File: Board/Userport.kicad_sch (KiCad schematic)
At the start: 8 parts, among them CN5 PORT_USER_PET_EDGE, X7 M09-182, X8 M09-182

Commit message: ultipet 1.1a board
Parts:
- removed JP18: JP2E, cbm_ultipet_v1:JP2, symbol cbm_ultipet_v1-eagle-import:JP2E
- added C147, C150: 0.1u, cbm_ultipet_v1:C0603, symbol cbm_ultipet_v1-eagle-import:C-EUC0603
- added U4, U5: CD4053B, Package_SO:TSSOP-16_4.4x5mm_P0.65mm, symbol Analog_Switch:CD4053B
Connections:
- net GND: now also C147.2, C150.2, U4.6 (INH), U4.7 (VEE), U4.8 (VSS), U5.6 (INH), U5.7 (VEE), U5.8 (VSS)
- net UP0: now also U5.13 (A1), U5.2 (B0); no longer X7.1
- net UP1: now also U4.1 (B1), U4.5 (C0); no longer X7.2
- net UP2: now also U5.1 (B1), U5.12 (A0); no longer X7.4
- net UP3: now also U4.2 (B0), U4.3 (C1); no longer X7.3
- net UP5: now also U4.13 (A1)
- net VCC: now also C147.1, C150.1, U4.16 (VDD), U5.16 (VDD)
- net at X7.6: now also U4.14 (A)
- net at D29.A, D30.A: now also U4.12 (A0)
- new net: U5.15 (B), X7.1
- new net: U4.4 (C), X7.2
- new net: U5.14 (A), X7.3
- new net: U4.15 (B), X7.4
- new net FUC2: U4.10 (S2), U4.11 (S1), U4.9 (S3), U5.10 (S2), U5.11 (S1), U5.9 (S3)
- new net OPENHIGH: U5.4 (C)
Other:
- note added: "1.1A: - switch between single/dual joystick config - switch Joy1/Joy2 on board"
- note added: "CBM-ULTIPET-V1.1A"
- note added: "CBM-ULTIPET-V1.1A-20240601"
- note added: "Down"
- note added: "Fire"
- note added: "High is single Joystick, Low is dual Joystick"
- note added: "Left"
- note added: "Right"
- note added: "Up"
- note added: "Use Female connectors!"
- note removed: "CBM-ULTIPET-V1.0A"
- note removed: "CBM-ULTIPET-V1.0A-20240104"
- moved on the sheet: D27, D28, D29, D30, X7, X8

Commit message: various fixes as documented in github issues
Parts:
- removed D27, D28, D29, D30: 1N4148DO35-10, cbm_ultipet_v1:DO35-10, symbol cbm_ultipet_v1-eagle-import:1N4148DO35-10
- added D12, D15, D16, D17: 1N4448, cbm_ultipet_v1:DO35-10, symbol cbm_ultipet_v1-eagle-import:1N4148DO35-10
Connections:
- net UP0: now also D12.A
- net UP1: now also D15.A
- net UP4: now also D16.A
- net UP5: now also D17.A
- net at X8.6: now also D16.C, D17.C
- net at U4.12 (A0): now also D12.C, D15.C
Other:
- note added: "1.1A: - switch between single/dual joystick config - switch Joy1/Joy2 on board 1.2A: - switch diodes direction to fix dual mode joystick fire - replace 1N4148 with 1N4448 due to lower fwd voltage"
- note added: "CBM-ULTIPET-V1.2A"
- note added: "CBM-ULTIPET-V1.2A-20241013"
- note added: "Male DB9 connectors"
- note removed: "1.1A: - switch between single/dual joystick config - switch Joy1/Joy2 on board"
- note removed: "CBM-ULTIPET-V1.1A"
- note removed: "CBM-ULTIPET-V1.1A-20240601"
- note removed: "Use Female connectors!"

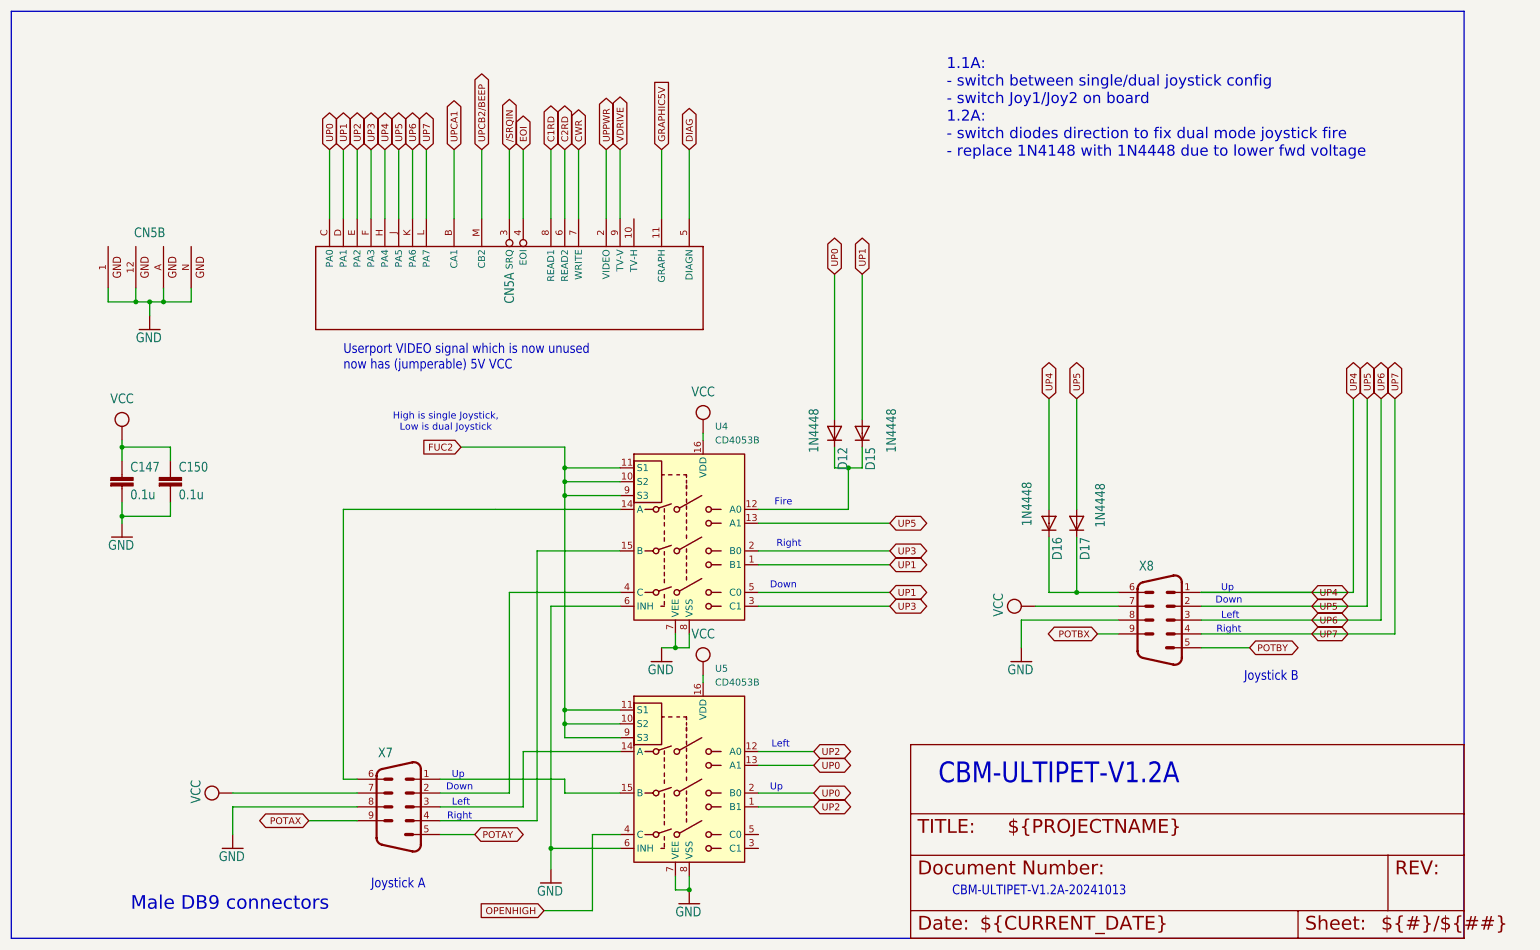
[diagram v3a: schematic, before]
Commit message: clamp diodes for joysticks
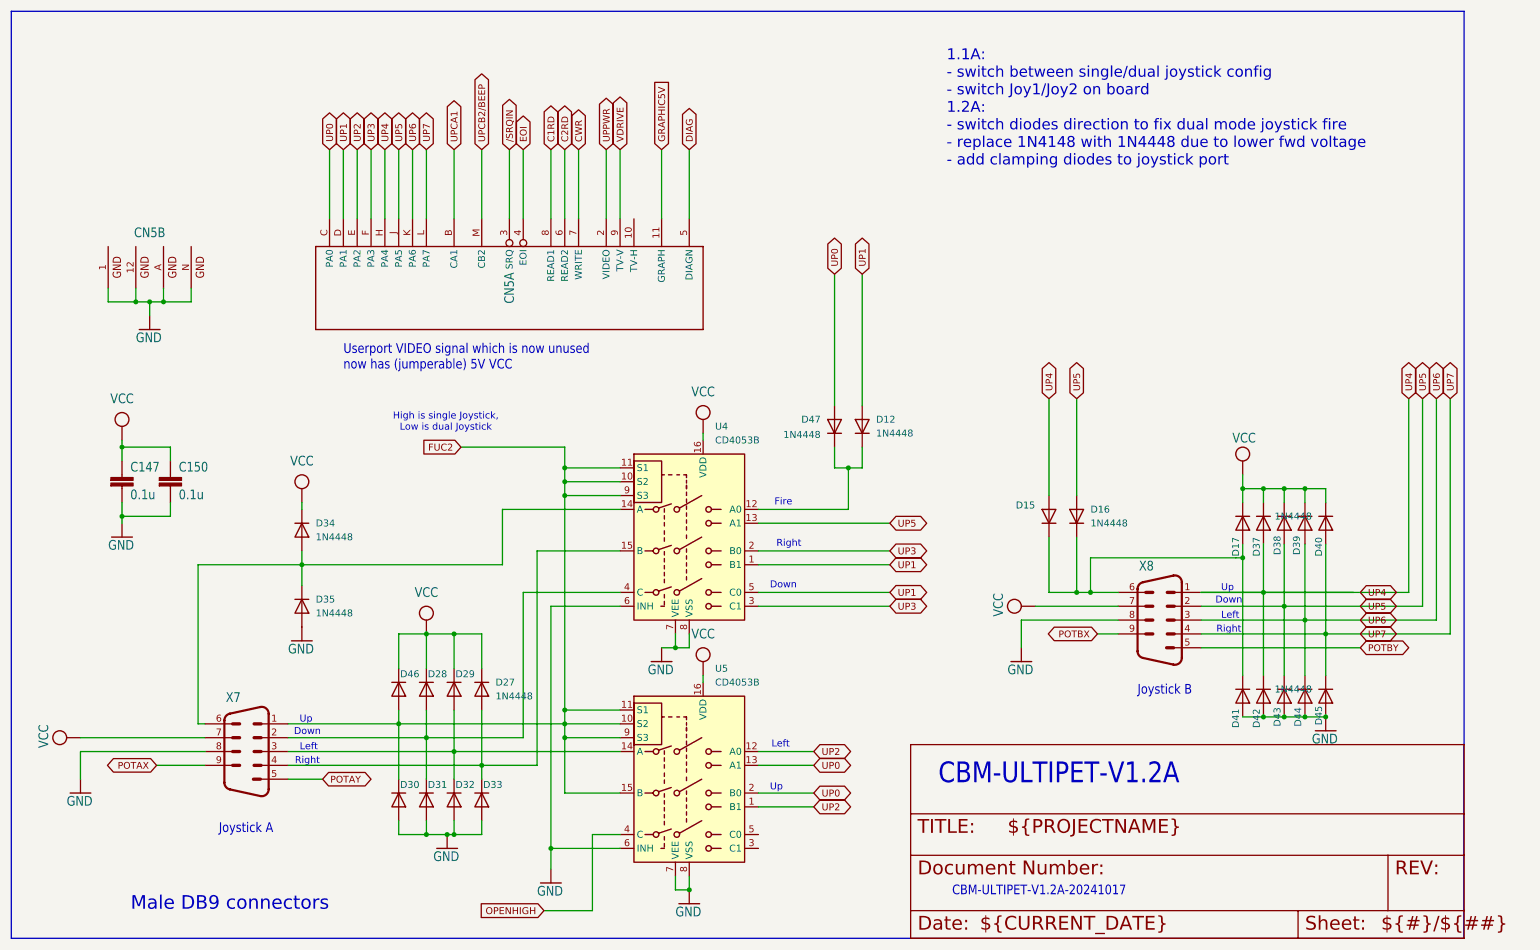
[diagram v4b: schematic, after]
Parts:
- removed D12, D15, D16, D17: 1N4448, cbm_ultipet_v1:DO35-10, symbol cbm_ultipet_v1-eagle-import:1N4148DO35-10
- added D12, D15, D16, D17, D27, D28, D29, D30, D31, D32, D33, D34, D35, D37, D38, D39, D40, D41, D42, D43, D44, D45, D46, D47: 1N4448, Diode_THT:D_DO-35_SOD27_P7.62mm_Horizontal, symbol Diode:1N4448
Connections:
- net FUC2: now also U5.15 (B), X7.1, D30.1 (K), D46.2 (A)
- net GND: now also D30.2 (A), D31.2 (A), D32.2 (A), D33.2 (A), D35.2 (A), D41.2 (A), D42.2 (A), D43.2 (A), D44.2 (A), D45.2 (A)
- net UP0: now also D47.2 (A)
- net UP1: now also D12.2 (A)
- net UP4: now also D15.2 (A), D37.2 (A), D42.1 (K)
- net UP5: now also D16.2 (A), D38.2 (A), D43.1 (K)
- net UP6: now also D39.2 (A), D44.1 (K)
- net UP7: now also D40.2 (A), D45.1 (K)
- net VCC: now also D17.1 (K), D27.1 (K), D28.1 (K), D29.1 (K), D34.1 (K), D37.1 (K), D38.1 (K), D39.1 (K), D40.1 (K), D46.1 (K)
- net at X8.6: now also D15.1 (K), D16.1 (K), D17.2 (A), D41.1 (K)
- net at U4.4 (C), X7.2: now also D28.2 (A), D31.1 (K)
- net at U5.14 (A), X7.3: now also D29.2 (A), D32.1 (K)
- net at U4.15 (B), X7.4: now also D27.2 (A), D33.1 (K)
- net at U4.14 (A), X7.6: now also D34.2 (A), D35.1 (K)
- net at U4.12 (A0): now also D12.1 (K), D47.1 (K)
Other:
- note added: "1.1A: - switch between single/dual joystick config - switch Joy1/Joy2 on board 1.2A: - switch diodes direction to fix dual mode joystick fire - replace 1N4148 with 1N4448 due to lower fwd voltage - add clamping diodes to joystick port"
- note added: "CBM-ULTIPET-V1.2A-20241017"
- note removed: "1.1A: - switch between single/dual joystick config - switch Joy1/Joy2 on board 1.2A: - switch diodes direction to fix dual mode joystick fire - replace 1N4148 with 1N4448 due to lower fwd voltage"
- note removed: "CBM-ULTIPET-V1.2A-20241013"
- moved on the sheet: X7

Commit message: more layout work
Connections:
- net FUC2: no longer D30.1 (K), D46.2 (A), U5.15 (B), X7.1
- new net: D30.1 (K), D46.2 (A), U5.15 (B), X7.1
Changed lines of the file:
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@@
-	)
-	(junction
-		(at 119.38 151.13)
-		(diameter 0)
-		(color 0 0 0 0)
 	)
 	(junction
@@
 	(wire
 		(pts
+			(xy 110.49 148.59) (xy 110.49 161.29)
+		)
+		(stroke
+			(width 0)
+			(type default)
+		)
+	)
+	(wire
+		(pts
 			(xy 38.1 110.49) (xy 38.1 111.76)
 		)
@@
 	(wire
 		(pts
-			(xy 119.38 151.13) (xy 119.38 161.29)
-		)
-		(stroke
-			(width 0)
-			(type default)
-		)
-	)
-	(wire
-		(pts
 			(xy 142.24 43.18) (xy 142.24 55.88)
 		)
@@
 	(wire
 		(pts
-			(xy 119.38 161.29) (xy 129.54 161.29)
-		)
-		(stroke
-			(width 0)
-			(type default)
-		)
-	)
-	(wire
-		(pts
 			(xy 99.06 168.91) (xy 104.14 168.91)
 		)
@@
 	(wire
 		(pts
-			(xy 88.9 148.59) (xy 119.38 148.59)
-		)
-		(stroke
-			(width 0)
-			(type default)
-		)
-	)
-	(wire
-		(pts
 			(xy 255.27 107.95) (xy 255.27 105.41)
 		)
@@
 	(wire
 		(pts
+			(xy 110.49 161.29) (xy 129.54 161.29)
+		)
+		(stroke
+			(width 0)
+			(type default)
+		)
+	)
+	(wire
+		(pts
 			(xy 259.08 115.57) (xy 259.08 132.08)
 		)
@@
 		)
 		(stroke
+			(width 0)
+			(type default)
+		)
+	)
+	(wire
+		(pts
+			(xy 88.9 148.59) (xy 110.49 148.59)
+		)
+		(stroke

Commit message: replace some ultipet specific TQFP with easier to solder parts
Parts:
- U4, U5: footprint Package_SO:TSSOP-16_4.4x5mm_P0.65mm -> Package_SO:SOIC-16_3.9x9.9mm_P1.27mm
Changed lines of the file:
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@@
 			)
 		)
-		(property "Footprint" "Package_SO:TSSOP-16_4.4x5mm_P0.65mm"
+		(property "Footprint" "Package_SO:SOIC-16_3.9x9.9mm_P1.27mm"
 			(at 146.05 177.8 0)
 			(effects
@@
 			)
 		)
-		(property "Footprint" "Package_SO:TSSOP-16_4.4x5mm_P0.65mm"
+		(property "Footprint" "Package_SO:SOIC-16_3.9x9.9mm_P1.27mm"
 			(at 146.05 133.35 0)
 			(effects

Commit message: work on r1.3
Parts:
- X7, X8: footprint cbm_ultipet_v1:182-009-MALE -> Connector_Dsub:DSUB-9_Pins_Horizontal_P2.77x2.84mm_EdgePinOffset9.90mm_Housed_MountingHolesOffset11.32mm
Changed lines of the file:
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@@
 			)
 		)
-		(property "Footprint" "cbm_ultipet_v1:182-009-MALE"
+		(property "Footprint" "Connector_Dsub:DSUB-9_Pins_Horizontal_P2.77x2.84mm_EdgePinOffset9.90mm_Housed_MountingHolesOffset11.32mm"
 			(at 60.96 153.67 0)
 			(effects
@@
 			)
 		)
-		(property "Footprint" "cbm_ultipet_v1:182-009-MALE"
+		(property "Footprint" "Connector_Dsub:DSUB-9_Pins_Horizontal_P2.77x2.84mm_EdgePinOffset9.90mm_Housed_MountingHolesOffset11.32mm"
 			(at 228.6 129.54 0)
 			(effects
